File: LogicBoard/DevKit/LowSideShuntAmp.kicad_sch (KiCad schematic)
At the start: 9 parts, among them U28 INA4181A1IPWR

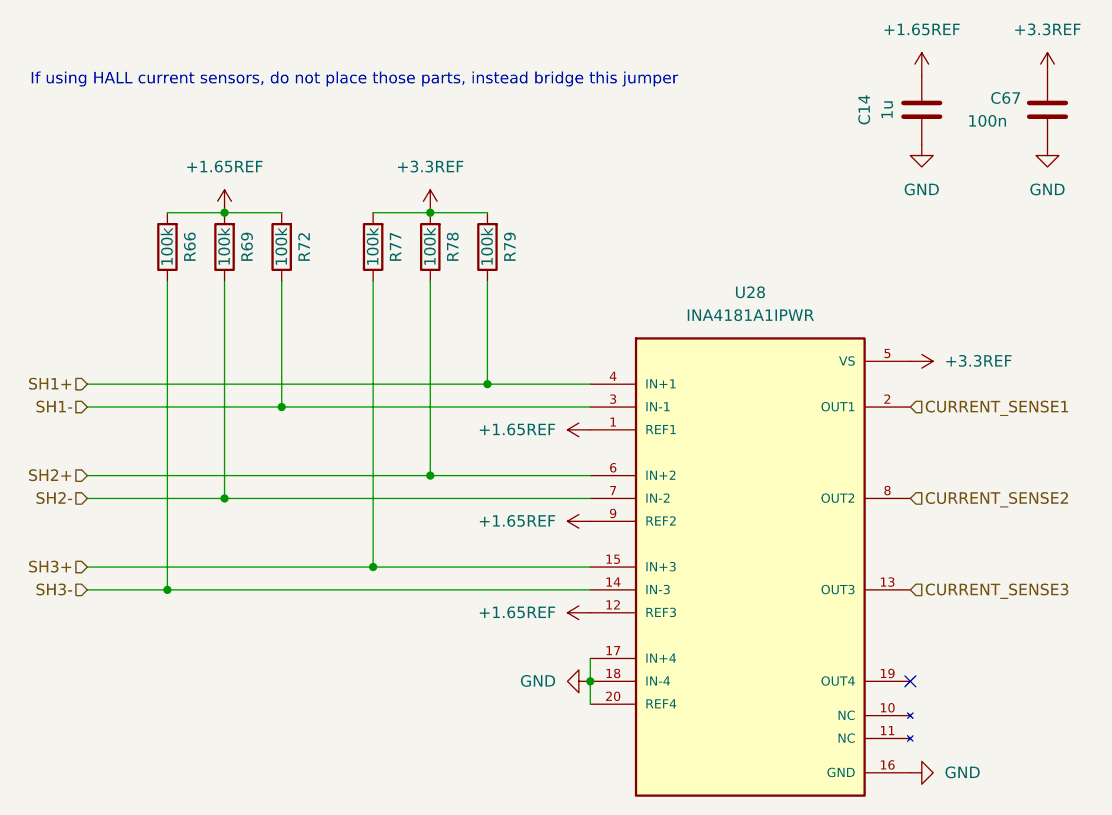
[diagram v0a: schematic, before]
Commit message: v2.9.0 - Small Hall/low side shunt
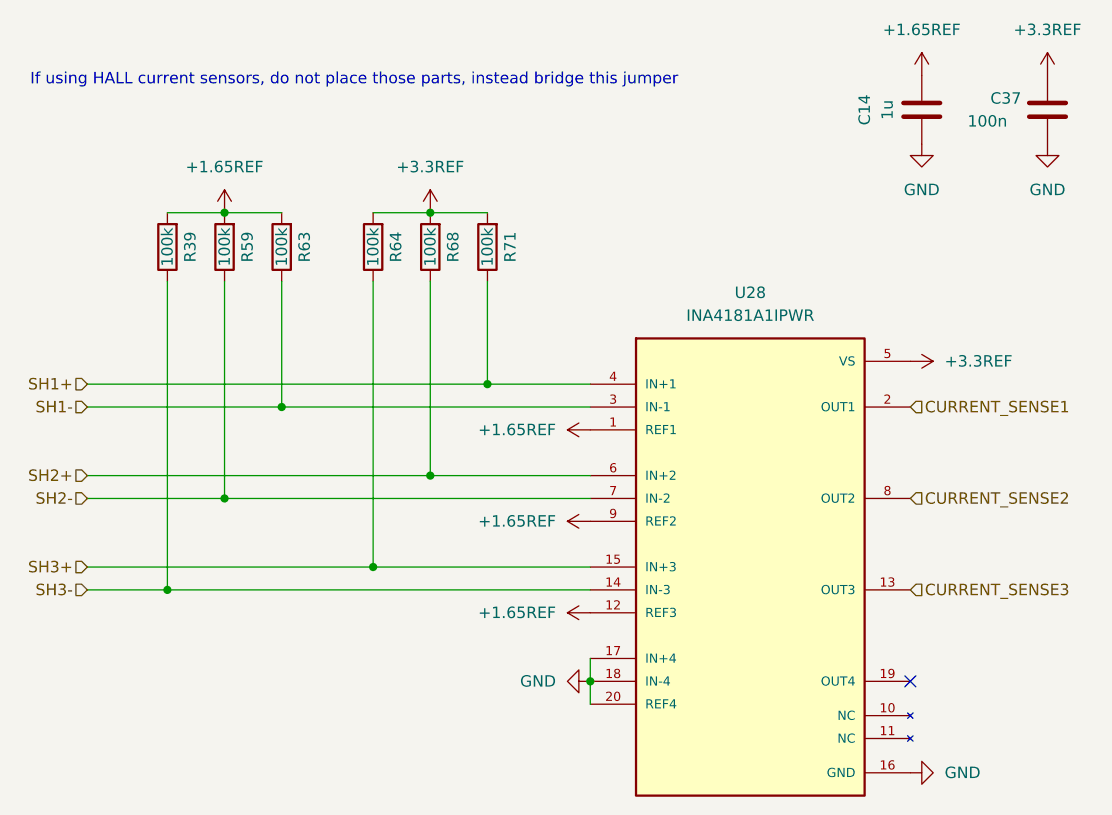
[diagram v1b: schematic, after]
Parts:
- renumbered C67 to C37, R66 to R39, R69 to R59, R72 to R63, R77 to R64, R78 to R68, R79 to R71
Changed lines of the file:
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@@
   (symbol (lib_id "Device:R") (at 93.98 81.28 180) (unit 1)
     (in_bom yes) (on_board yes) (dnp no)
-    (property "Reference" "R66" (at 96.52 81.28 90)
+    (property "Reference" "R39" (at 96.52 81.28 90)
       (effects (font (size 1.27 1.27)))
     )
@@
   (symbol (lib_id "Device:R") (at 123.19 81.28 180) (unit 1)
     (in_bom yes) (on_board yes) (dnp no)
-    (property "Reference" "R78" (at 125.73 81.28 90)
+    (property "Reference" "R68" (at 125.73 81.28 90)
       (effects (font (size 1.27 1.27)))
     )
@@
   (symbol (lib_id "Device:R") (at 116.84 81.28 180) (unit 1)
     (in_bom yes) (on_board yes) (dnp no)
-    (property "Reference" "R77" (at 119.38 81.28 90)
+    (property "Reference" "R64" (at 119.38 81.28 90)
       (effects (font (size 1.27 1.27)))
     )
@@
   (symbol (lib_id "Device:R") (at 100.33 81.28 180) (unit 1)
     (in_bom yes) (on_board yes) (dnp no)
-    (property "Reference" "R69" (at 102.87 81.28 90)
+    (property "Reference" "R59" (at 102.87 81.28 90)
       (effects (font (size 1.27 1.27)))
     )
@@
   (symbol (lib_id "Device:C") (at 191.77 66.04 0) (unit 1)
     (in_bom yes) (on_board yes) (dnp no)
-    (property "Reference" "C67" (at 185.42 64.77 0)
+    (property "Reference" "C37" (at 185.42 64.77 0)
       (effects (font (size 1.27 1.27)) (justify left))
     )
@@
   (symbol (lib_id "Device:R") (at 106.68 81.28 180) (unit 1)
     (in_bom yes) (on_board yes) (dnp no)
-    (property "Reference" "R72" (at 109.22 81.28 90)
+    (property "Reference" "R63" (at 109.22 81.28 90)
       (effects (font (size 1.27 1.27)))
     )
@@
   (symbol (lib_id "Device:R") (at 129.54 81.28 180) (unit 1)
     (in_bom yes) (on_board yes) (dnp no)
-    (property "Reference" "R79" (at 132.08 81.28 90)
+    (property "Reference" "R71" (at 132.08 81.28 90)
       (effects (font (size 1.27 1.27)))
     )
@@
   (symbol (lib_id "power:GND") (at 176.53 139.7 90) (unit 1)
     (in_bom yes) (on_board yes) (dnp no) (fields_autoplaced)
-    (property "Reference" "#PWR0189" (at 182.88 139.7 0)
-      (effects (font (size 1.27 1.27)) hide)
-    )
+    (property "Reference" "#PWR0167" (at 182.88 139.7 0)
+      (effects (font (size 1.27 1.27)) hide)
+    )
